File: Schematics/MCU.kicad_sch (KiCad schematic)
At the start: 27 parts, among them J1 Microsemi_FlashPro-JTAG-10, U3 STM32F405RGT6, Y1 8mhz

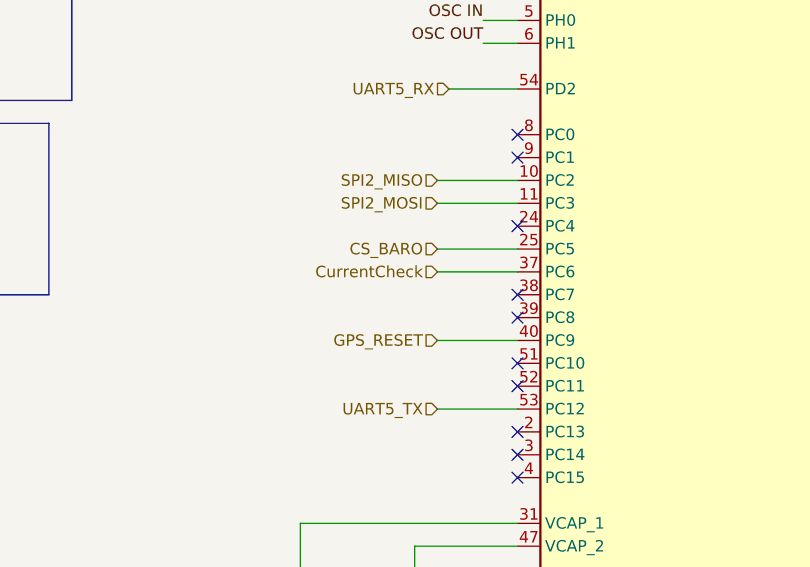
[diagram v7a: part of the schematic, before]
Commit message: Added encoder connection for parafoil motor position information, in buy order ready for purchase
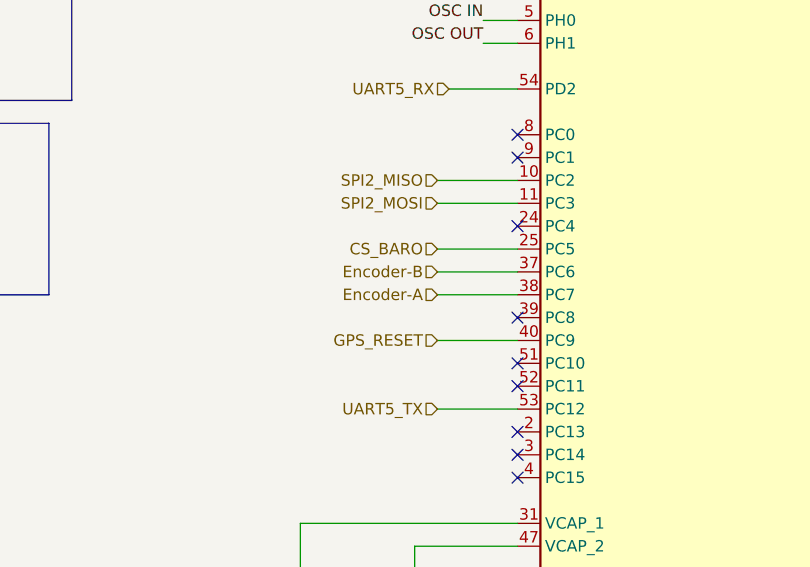
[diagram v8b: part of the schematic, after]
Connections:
- net Encoder-A: now reaches U3.38 (PC7)
- net CurrentCheck renamed Encoder-B
- no-connect marks 33 -> 32
